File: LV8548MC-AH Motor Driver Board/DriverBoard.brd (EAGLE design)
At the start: 17.2 x 17.9 mm, 6 parts, among them U1 DRIVER-LV8548MC-AH(SOIC10), U2 DRIVER-LV8548MC-AH(SOIC10)

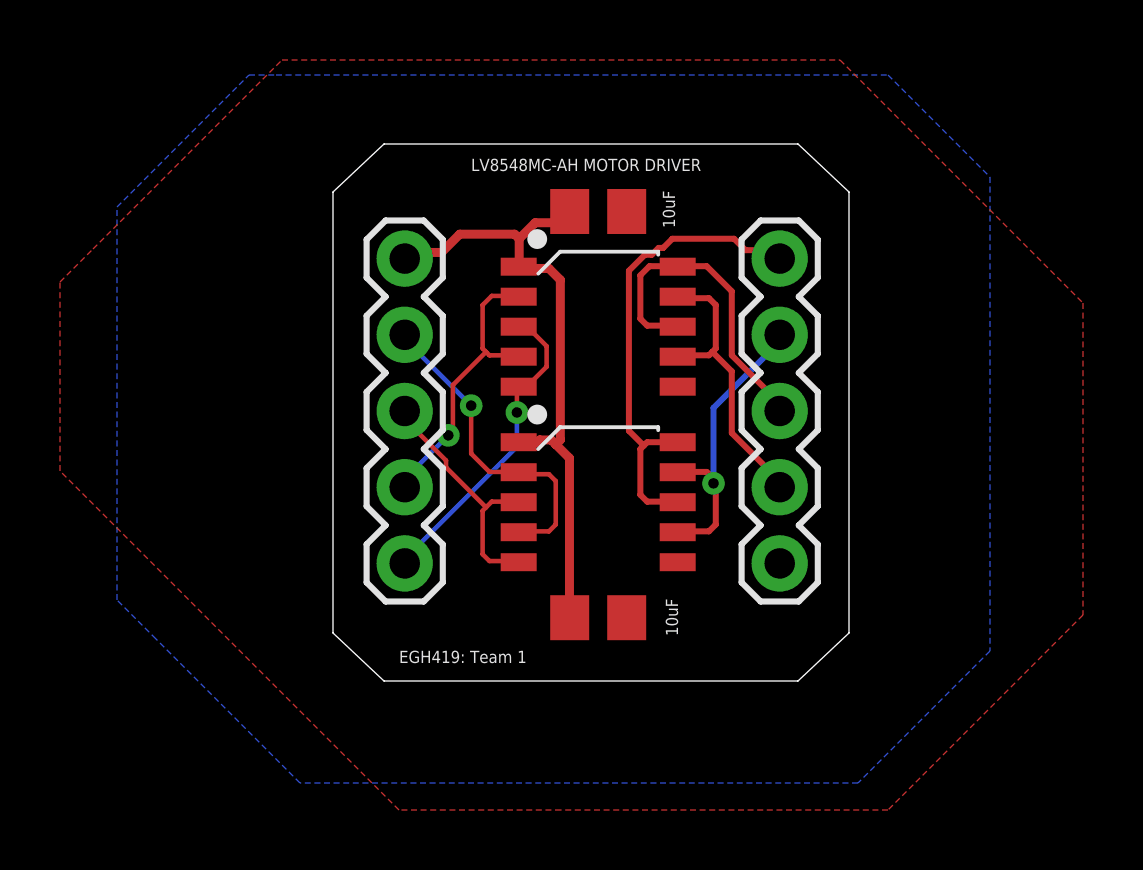
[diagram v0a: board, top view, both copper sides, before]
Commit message: Added Breakout Board2
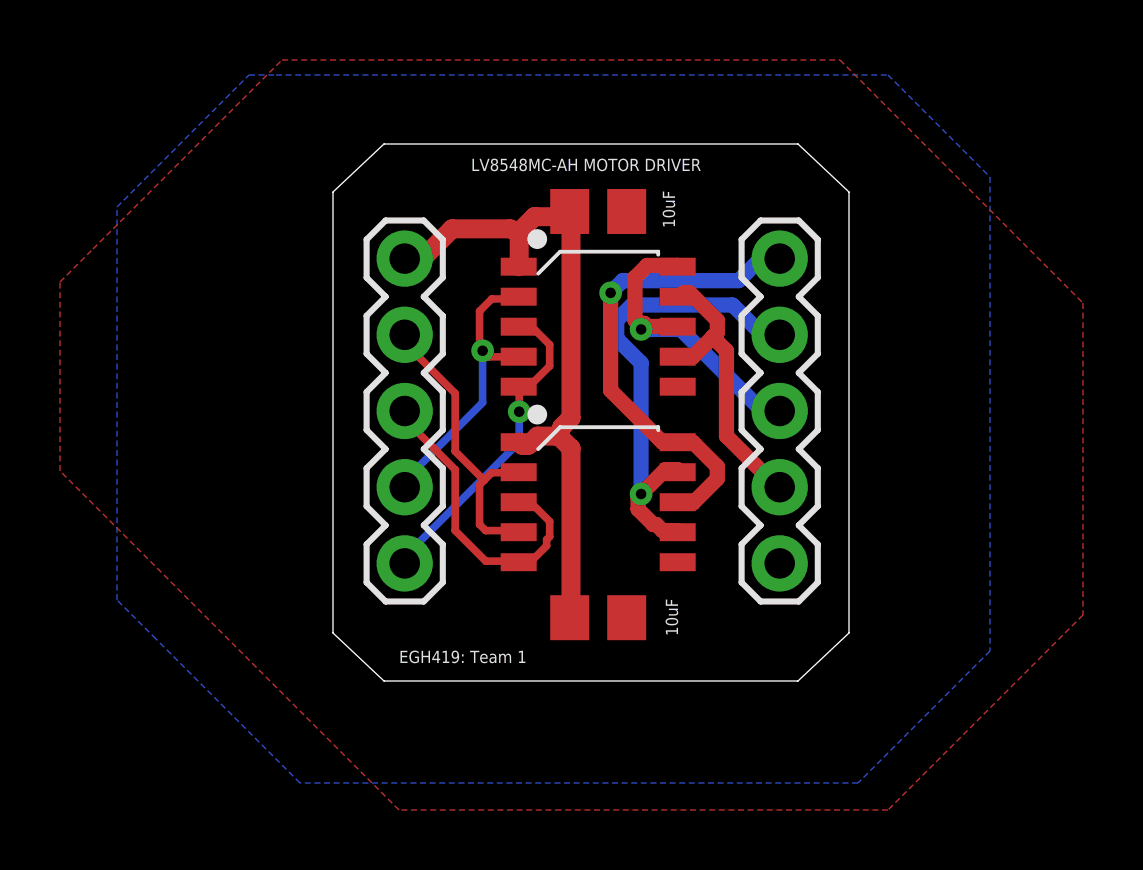
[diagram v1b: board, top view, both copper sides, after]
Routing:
- net M1_OUT2: track 10.2 -> 16.1 mm
- net M1B: track 8.42 -> 10.6 mm
- net VCC: track 21.7 -> 22.8 mm
- net M1A: track 10.9 -> 10.2 mm, vias 1 -> 0
- net M2_OUT1: track 11.0 -> 10.6 mm, vias 0 -> 1
- net M1_OUT1: vias 0 -> 1
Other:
- board text added: "C:/Users/CodyS/OneDrive - Queensland University of Technology/Uni Coursework/2021/EGH419 Group 1 Shared Folder/Git Stuff/EGH419/LOGO.bmp"
